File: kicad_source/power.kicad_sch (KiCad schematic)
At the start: 45 parts, among them CN1 DNI, CN2 SM04B-GHS-TB, CN3 SM04B-GHS-TB, CN4 Powerpole_2, CN5 SM04B-GHS-TB, CN6 SM04B-GHS-TB, CN7 DNI, U1 RAA211650

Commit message: reworked schematic
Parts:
- removed C11, C9: 100 nF, Capacitor_SMD:C_0603_1608Metric, symbol Device:C_Small
- removed CN2, CN3, CN5, CN6: SM04B-GHS-TB, Connector_JST:JST_GH_SM04B-GHS-TB_1x04-1MP_P1.25mm_Horizontal, symbol Connector_Generic_MountingPin:Conn_01x04_MountingPin
- removed D1, D2: B520C, Diode_SMD:D_SMC, symbol Device:D_Schottky_Small
- removed H1, H2, H3, H4: MountingHole_Pad, MountingHole:MountingHole_3.2mm_M3_DIN965_Pad, symbol Mechanical:MountingHole_Pad
- removed L2: Label, generationmake:generationmake_logo, symbol generationmake:Label
- removed L3: Label, generationmake:generationmake_small_solder, symbol generationmake:Label
- removed L4: Label, generationmake:opencyphal_small, symbol generationmake:Label
- added D?: MBR0530T1G, Diode_SMD:D_SOD-123, symbol Device:D_Schottky_Small
- renumbered C17 to C13, C1 to C14, C2 to C15, C3 to C16, C12 to C17, C4 to C18, C13 to C19, C5 to C20, C6 to C21, C14 to C22, C15 to C23, C7 to C24, C16 to C25, C8 to C26, C10 to C27, CN1 to CN10, CN7 to CN13, CN4 to CN9, D4 to D1, L1 to L4, R5 to R26, R6 to R27, R1 to R28, R2 to R29, R3 to R30, R7 to R31, R8 to R32, R4 to R33
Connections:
- net VCC: now also D?.2 (A)
- new net +5V: D?.1 (K)
- no-connect marks 4 -> 0
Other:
- note added: "30V 500mA"
- company: 107-systems -> generationmake
- title: l3xz-hw_can_power_injector -> OpenCyphalServoController12
- moved on the sheet: C26, C27, D3, R33

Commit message: started first placement
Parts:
- removed C23: 220 uF / 50 V, Capacitor_SMD:CP_Elec_10x10, symbol Device:C_Polarized_Small
- C13: renamed from C17; value 220 uF / 50 V -> 100 uF / 50 V; footprint Capacitor_SMD:CP_Elec_10x10 -> Capacitor_SMD:CP_Elec_8x10
- C15: renamed from C19; value 220 uF / 50 V -> 100 uF / 50 V; footprint Capacitor_SMD:CP_Elec_10x10 -> Capacitor_SMD:CP_Elec_8x10
- gave numbers to parts that had none: 1
- renumbered C14 to C10, C15 to C11, C16 to C12, C18 to C14, C20 to C16, C21 to C17, C22 to C18, C24 to C20, C25 to C21, C26 to C22, C27 to C23, C13 to C9, CN9 to CN12, CN10 to CN13, CN13 to CN14, D1 to D4, D3 to D5, U1 to U4
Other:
- note added: "ECC ZA500101MHA"
- note removed: "ECC MZL500ARA221 EMZL500ARA221MJA0G"

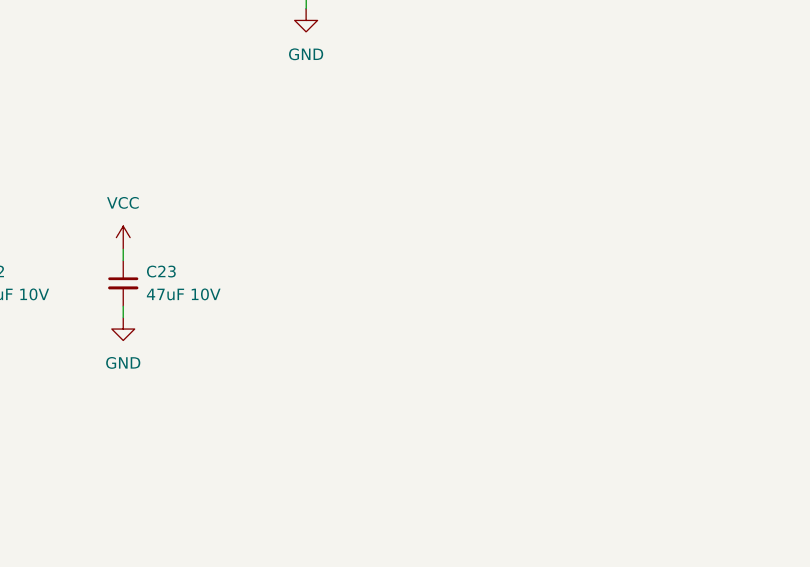
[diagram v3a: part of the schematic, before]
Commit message: added additional capacitors on VCC
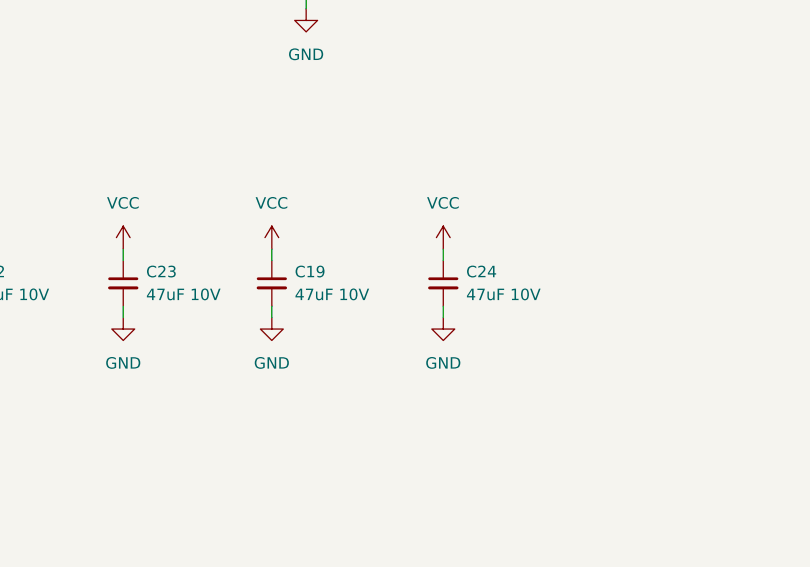
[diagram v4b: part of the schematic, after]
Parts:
- added C19, C24: 47uF 10V, Capacitor_SMD:C_1210_3225Metric, symbol Device:C_Small
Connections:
- net GND: now also C19.2, C24.2
- net VCC: now also C19.1, C24.1
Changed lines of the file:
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@@
+    (stroke (width 0) (type default) (color 0 0 0 0))
+  )
+  (wire (pts (xy 207.01 71.12) (xy 207.01 72.39))
     (stroke (width 0) (type default) (color 0 0 0 0))
   )
@@
     (stroke (width 0) (type default) (color 0 0 0 0))
   )
+  (wire (pts (xy 187.96 71.12) (xy 187.96 72.39))
+    (stroke (width 0) (type default) (color 0 0 0 0))
+  )
   (wire (pts (xy 86.36 24.13) (xy 86.36 25.4))
     (stroke (width 0) (type default) (color 0 0 0 0))
@@
     (stroke (width 0) (type default) (color 0 0 0 0))
   )
+  (wire (pts (xy 207.01 77.47) (xy 207.01 78.74))
+    (stroke (width 0) (type default) (color 0 0 0 0))
+  )
   (wire (pts (xy 86.36 30.48) (xy 86.36 31.75))
     (stroke (width 0) (type default) (color 0 0 0 0))
@@
   )
   (wire (pts (xy 100.33 87.63) (xy 97.79 87.63))
+    (stroke (width 0) (type default) (color 0 0 0 0))
+  )
+  (wire (pts (xy 187.96 77.47) (xy 187.96 78.74))
     (stroke (width 0) (type default) (color 0 0 0 0))
   )
@@
     (pin "1")
   )
+  (symbol (lib_id "power:VCC") (at 187.96 71.12 0) (unit 1)
+    (in_bom yes) (on_board yes) (fields_autoplaced)
+    (property "Reference" "#PWR088" (id 0) (at 187.96 74.93 0)
+      (effects (font (size 1.27 1.27)) hide)
+    )
+    (property "Value" "VCC" (id 1) (at 187.96 66.04 0))
+    (property "Footprint" "" (id 2) (at 187.96 71.12 0)
+      (effects (font (size 1.27 1.27)) hide)
+    )
+    (property "Datasheet" "" (id 3) (at 187.96 71.12 0)
+      (effects (font (size 1.27 1.27)) hide)
+    )
+    (pin "1")
+  )
   (symbol (lib_id "power:GND") (at 97.79 100.33 0) (unit 1)
     (in_bom yes) (on_board yes) (fields_autoplaced)
@@
     (pin "1")
   )
+  (symbol (lib_id "power:GND") (at 207.01 78.74 0) (unit 1)
+    (in_bom yes) (on_board yes) (fields_autoplaced)
+    (property "Reference" "#PWR0105" (id 0) (at 207.01 85.09 0)
+      (effects (font (size 1.27 1.27)) hide)
+    )
+    (property "Value" "GND" (id 1) (at 207.01 83.82 0))
+    (property "Footprint" "" (id 2) (at 207.01 78.74 0)
+      (effects (font (size 1.27 1.27)) hide)
+    )
+    (property "Datasheet" "" (id 3) (at 207.01 78.74 0)
+      (effects (font (size 1.27 1.27)) hide)
+    )
+    (pin "1")
+  )
   (symbol (lib_id "Device:C_Small") (at 118.11 44.45 0) (unit 1)
     (in_bom yes) (on_board yes) (fields_autoplaced)
@@
     )
     (property "Datasheet" "" (id 3) (at 54.61 57.15 0)
+      (effects (font (size 1.27 1.27)) hide)
+    )
+    (pin "1")
+  )
+  (symbol (lib_id "power:GND") (at 187.96 78.74 0) (unit 1)
+    (in_bom yes) (on_board yes) (fields_autoplaced)
+    (property "Reference" "#PWR089" (id 0) (at 187.96 85.09 0)
+      (effects (font (size 1.27 1.27)) hide)
+    )
+    (property "Value" "GND" (id 1) (at 187.96 83.82 0))
+    (property "Footprint" "" (id 2) (at 187.96 78.74 0)
+      (effects (font (size 1.27 1.27)) hide)
+    )
+    (property "Datasheet" "" (id 3) (at 187.96 78.74 0)
       (effects (font (size 1.27 1.27)) hide)
     )
@@
     (pin "1")
     (pin "2")
+  )
+  (symbol (lib_id "power:VCC") (at 207.01 71.12 0) (unit 1)
+    (in_bom yes) (on_board yes) (fields_autoplaced)
+    (property "Reference" "#PWR0104" (id 0) (at 207.01 74.93 0)
+      (effects (font (size 1.27 1.27)) hide)
+    )
+    (property "Value" "VCC" (id 1) (at 207.01 66.04 0))
+    (property "Footprint" "" (id 2) (at 207.01 71.12 0)
+      (effects (font (size 1.27 1.27)) hide)
+    )
+    (property "Datasheet" "" (id 3) (at 207.01 71.12 0)
+      (effects (font (size 1.27 1.27)) hide)
+    )
+    (pin "1")
   )
   (symbol (lib_id "power:GND") (at 107.95 31.75 0) (unit 1)
@@
     (pin "2")
   )
+  (symbol (lib_id "Device:C_Small") (at 187.96 74.93 0) (unit 1)
+    (in_bom yes) (on_board yes) (fields_autoplaced)
+    (property "Reference" "C19" (id 0) (at 190.5 73.6662 0)
+      (effects (font (size 1.27 1.27)) (justify left))
+    )
+    (property "Value" "47uF 10V" (id 1) (at 190.5 76.2062 0)
+      (effects (font (size 1.27 1.27)) (justify left))
+    )
+    (property "Footprint" "Capacitor_SMD:C_1210_3225Metric" (id 2) (at 187.96 74.93 0)
+      (effects (font (size 1.27 1.27)) hide)
+    )
+    (property "Datasheet" "~" (id 3) (at 187.96 74.93 0)
+      (effects (font (size 1.27 1.27)) hide)
+    )
+    (pin "1")
+    (pin "2")
+  )
   (symbol (lib_id "power:GND") (at 55.88 93.98 0) (unit 1)
     (in_bom yes) (on_board yes) (fields_autoplaced)
@@
       (effects (font (size 1.27 1.27)) hide)
     )
+    (pin "1")
+    (pin "2")
+  )
+  (symbol (lib_id "Device:C_Small") (at 207.01 74.93 0) (unit 1)
+    (in_bom yes) (on_board yes) (fields_autoplaced)
+    (property "Reference" "C24" (id 0) (at 209.55 73.6662 0)
+      (effects (font (size 1.27 1.27)) (justify left))
+    )
+    (property "Value" "47uF 10V" (id 1) (at 209.55 76.2062 0)
+      (effects (font (size 1.27 1.27)) (justify left))
+    )
+    (property "Footprint" "Capacitor_SMD:C_1210_3225Metric" (id 2) (at 207.01 74.93 0)
+      (effects (font (size 1.27 1.27)) hide)
+    )
+    (property "Datasheet" "~" (id 3) (at 207.01 74.93 0)
+      (effects (font (size 1.27 1.27)) hide)
+    )

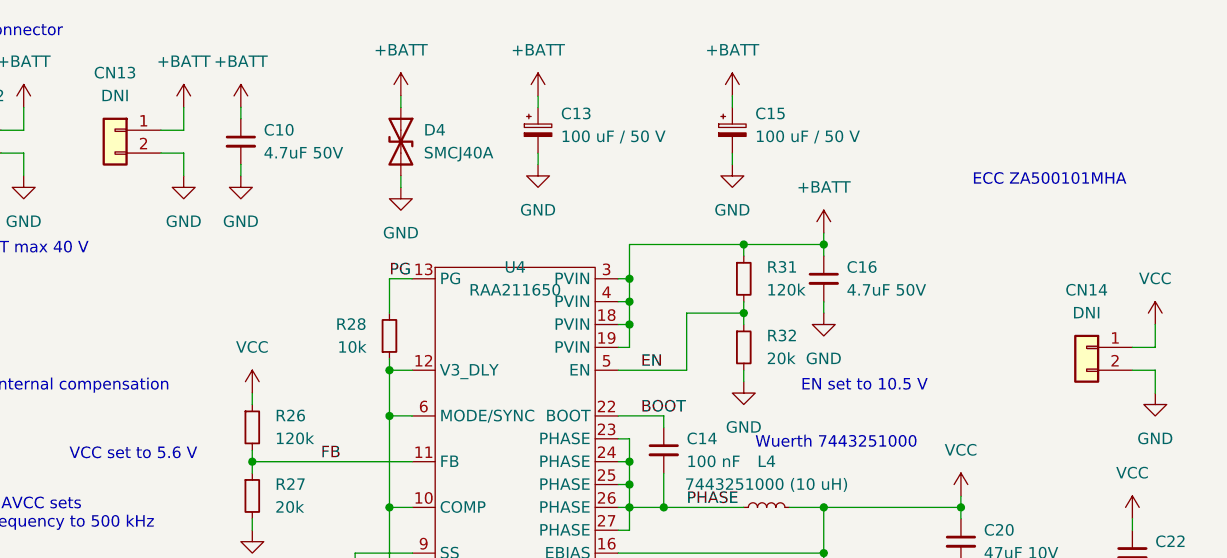
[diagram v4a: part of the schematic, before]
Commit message: added enable and power good for voltage regulator
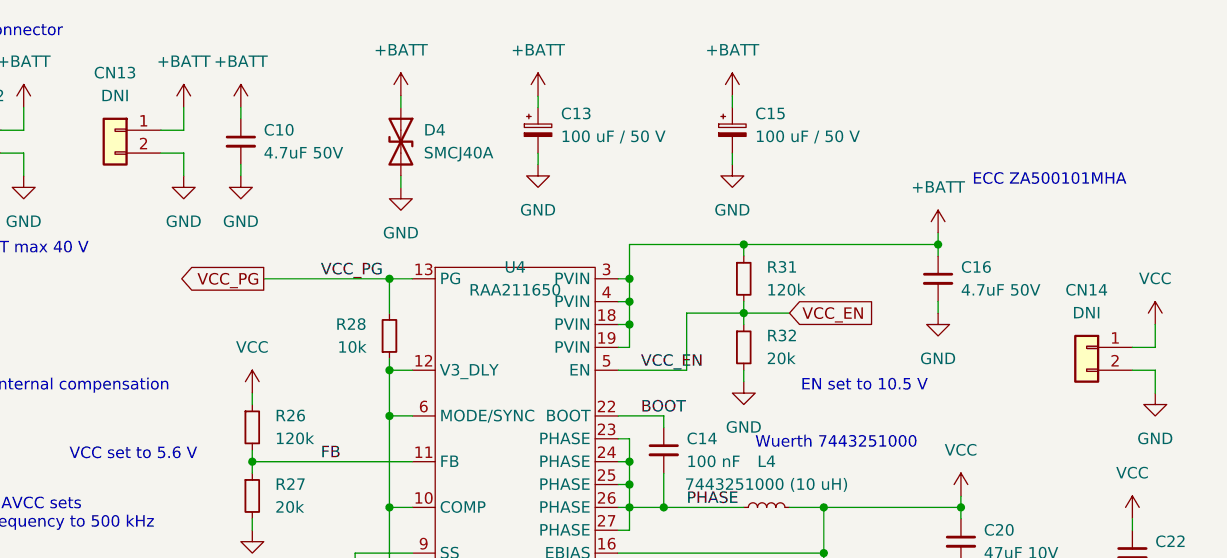
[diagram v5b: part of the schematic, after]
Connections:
- net EN renamed VCC_EN
- net PG renamed VCC_PG
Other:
- moved on the sheet: C16
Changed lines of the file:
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@@
   (junction (at 69.85 80.01) (diameter 0) (color 0 0 0 0)
   )
-  (junction (at 118.11 40.64) (diameter 0) (color 0 0 0 0)
+  (junction (at 130.81 40.64) (diameter 0) (color 0 0 0 0)
   )
   (junction (at 97.79 90.17) (diameter 0) (color 0 0 0 0)
@@
   (junction (at 118.11 69.85) (diameter 0) (color 0 0 0 0)
   )
+  (junction (at 100.33 69.85) (diameter 0) (color 0 0 0 0)
+  )
+  (junction (at 96.52 44.45) (diameter 0) (color 0 0 0 0)
+  )
+  (junction (at 96.52 64.77) (diameter 0) (color 0 0 0 0)
+  )
+  (junction (at 97.79 87.63) (diameter 0) (color 0 0 0 0)
+  )
+  (junction (at 69.85 44.45) (diameter 0) (color 0 0 0 0)
+  )
+  (junction (at 96.52 67.31) (diameter 0) (color 0 0 0 0)
+  )
+  (junction (at 133.35 69.85) (diameter 0) (color 0 0 0 0)
+  )
+  (junction (at 97.79 95.25) (diameter 0) (color 0 0 0 0)
+  )
+  (junction (at 69.85 59.69) (diameter 0) (color 0 0 0 0)
+  )
+  (junction (at 118.11 74.93) (diameter 0) (color 0 0 0 0)
+  )
+  (junction (at 97.79 85.09) (diameter 0) (color 0 0 0 0)
+  )
+  (junction (at 97.79 92.71) (diameter 0) (color 0 0 0 0)
+  )
+  (junction (at 97.79 97.79) (diameter 0) (color 0 0 0 0)
+  )
   (junction (at 109.22 40.64) (diameter 0) (color 0 0 0 0)
   )
-  (junction (at 100.33 69.85) (diameter 0) (color 0 0 0 0)
-  )
-  (junction (at 96.52 44.45) (diameter 0) (color 0 0 0 0)
-  )
-  (junction (at 96.52 64.77) (diameter 0) (color 0 0 0 0)
-  )
-  (junction (at 97.79 87.63) (diameter 0) (color 0 0 0 0)
-  )
-  (junction (at 96.52 67.31) (diameter 0) (color 0 0 0 0)
-  )
-  (junction (at 133.35 69.85) (diameter 0) (color 0 0 0 0)
-  )
-  (junction (at 97.79 95.25) (diameter 0) (color 0 0 0 0)
-  )
-  (junction (at 69.85 59.69) (diameter 0) (color 0 0 0 0)
-  )
-  (junction (at 118.11 74.93) (diameter 0) (color 0 0 0 0)
-  )
-  (junction (at 97.79 85.09) (diameter 0) (color 0 0 0 0)
-  )
-  (junction (at 97.79 92.71) (diameter 0) (color 0 0 0 0)
-  )
-  (junction (at 97.79 97.79) (diameter 0) (color 0 0 0 0)
-  )
   (junction (at 96.52 46.99) (diameter 0) (color 0 0 0 0)
   )
@@
     (stroke (width 0) (type default) (color 0 0 0 0))
   )
-  (wire (pts (xy 118.11 40.64) (xy 118.11 41.91))
+  (wire (pts (xy 130.81 40.64) (xy 130.81 41.91))
     (stroke (width 0) (type default) (color 0 0 0 0))
   )
@@
     (stroke (width 0) (type default) (color 0 0 0 0))
   )
-  (wire (pts (xy 118.11 46.99) (xy 118.11 48.26))
+  (wire (pts (xy 130.81 46.99) (xy 130.81 48.26))
     (stroke (width 0) (type default) (color 0 0 0 0))
   )
@@
     (stroke (width 0) (type default) (color 0 0 0 0))
   )
+  (wire (pts (xy 109.22 48.26) (xy 114.3 48.26))
+    (stroke (width 0) (type default) (color 0 0 0 0))
+  )
   (wire (pts (xy 55.88 85.09) (xy 69.85 85.09))
     (stroke (width 0) (type default) (color 0 0 0 0))
@@
     (stroke (width 0) (type default) (color 0 0 0 0))
   )
+  (wire (pts (xy 55.88 44.45) (xy 69.85 44.45))
+    (stroke (width 0) (type default) (color 0 0 0 0))
+  )
   (wire (pts (xy 118.11 74.93) (xy 118.11 76.2))
     (stroke (width 0) (type default) (color 0 0 0 0))
@@
     (stroke (width 0) (type default) (color 0 0 0 0))
   )
-  (wire (pts (xy 118.11 39.37) (xy 118.11 40.64))
+  (wire (pts (xy 130.81 39.37) (xy 130.81 40.64))
     (stroke (width 0) (type default) (color 0 0 0 0))
   )
@@
     (stroke (width 0) (type default) (color 0 0 0 0))
   )
-  (wire (pts (xy 109.22 40.64) (xy 118.11 40.64))
+  (wire (pts (xy 109.22 40.64) (xy 130.81 40.64))
     (stroke (width 0) (type default) (color 0 0 0 0))
   )
@@
     (effects (font (size 1.27 1.27)) (justify left bottom))
   )
-  (label "EN" (at 97.79 54.61 0)
+  (label "VCC_EN" (at 97.79 54.61 0)
     (effects (font (size 1.27 1.27)) (justify left bottom))
   )
@@
     (effects (font (size 1.27 1.27)) (justify left bottom))
   )
-  (label "PG" (at 69.85 44.45 0)
+  (label "VCC_PG" (at 62.23 44.45 0)
     (effects (font (size 1.27 1.27)) (justify left bottom))
   )
@@
   (label "SS" (at 57.15 81.28 0)
     (effects (font (size 1.27 1.27)) (justify left bottom))
+  )
+  (global_label "VCC_PG" (shape output) (at 55.88 44.45 180) (fields_autoplaced)
+    (effects (font (size 1.27 1.27)) (justify right))
+    (property "Referenzen zwischen Schaltplänen" "${INTERSHEET_REFS}" (id 0) (at 46.4196 44.3706 0)
+      (effects (font (size 1.27 1.27)) (justify right) hide)
+    )
+  )
+  (global_label "VCC_EN" (shape input) (at 114.3 48.26 0) (fields_autoplaced)
+    (effects (font (size 1.27 1.27)) (justify left))
+    (property "Referenzen zwischen Schaltplänen" "${INTERSHEET_REFS}" (id 0) (at 123.6999 48.1806 0)
+      (effects (font (size 1.27 1.27)) (justify left) hide)
+    )
   )
   (symbol (lib_id "Device:C_Small") (at 55.88 90.17 0) (mirror x) (unit 1)
@@
     (pin "2")
   )
-  (symbol (lib_id "power:GND") (at 118.11 48.26 0) (unit 1)
-    (in_bom yes) (on_board yes) (fields_autoplaced)
-    (property "Reference" "#PWR084" (id 0) (at 118.11 54.61 0)
-      (effects (font (size 1.27 1.27)) hide)
-    )
-    (property "Value" "GND" (id 1) (at 118.11 53.34 0))
-    (property "Footprint" "" (id 2) (at 118.11 48.26 0)
-      (effects (font (size 1.27 1.27)) hide)
-    )
-    (property "Datasheet" "" (id 3) (at 118.11 48.26 0)
+  (symbol (lib_id "power:GND") (at 130.81 48.26 0) (unit 1)
+    (in_bom yes) (on_board yes) (fields_autoplaced)
+    (property "Reference" "#PWR084" (id 0) (at 130.81 54.61 0)
+      (effects (font (size 1.27 1.27)) hide)
+    )
+    (property "Value" "GND" (id 1) (at 130.81 53.34 0))
+    (property "Footprint" "" (id 2) (at 130.81 48.26 0)
+      (effects (font (size 1.27 1.27)) hide)
+    )
+    (property "Datasheet" "" (id 3) (at 130.81 48.26 0)
       (effects (font (size 1.27 1.27)) hide)
     )
@@
     (pin "1")
   )
-  (symbol (lib_id "Device:C_Small") (at 118.11 44.45 0) (unit 1)
-    (in_bom yes) (on_board yes) (fields_autoplaced)
-    (property "Reference" "C16" (id 0) (at 120.65 43.1862 0)
-      (effects (font (size 1.27 1.27)) (justify left))
-    )
-    (property "Value" "4.7uF 50V" (id 1) (at 120.65 45.7262 0)
-      (effects (font (size 1.27 1.27)) (justify left))
-    )
-    (property "Footprint" "Capacitor_SMD:C_1210_3225Metric" (id 2) (at 118.11 44.45 0)
-      (effects (font (size 1.27 1.27)) hide)
-    )
-    (property "Datasheet" "~" (id 3) (at 118.11 44.45 0)
+  (symbol (lib_id "Device:C_Small") (at 130.81 44.45 0) (unit 1)
+    (in_bom yes) (on_board yes) (fields_autoplaced)
+    (property "Reference" "C16" (id 0) (at 133.35 43.1862 0)
+      (effects (font (size 1.27 1.27)) (justify left))
+    )
+    (property "Value" "4.7uF 50V" (id 1) (at 133.35 45.7262 0)
+      (effects (font (size 1.27 1.27)) (justify left))
+    )
+    (property "Footprint" "Capacitor_SMD:C_1210_3225Metric" (id 2) (at 130.81 44.45 0)
+      (effects (font (size 1.27 1.27)) hide)
+    )
+    (property "Datasheet" "~" (id 3) (at 130.81 44.45 0)
       (effects (font (size 1.27 1.27)) hide)
     )
@@
     (pin "1")
   )
-  (symbol (lib_id "power:+BATT") (at 118.11 39.37 0) (unit 1)
-    (in_bom yes) (on_board yes) (fields_autoplaced)
-    (property "Reference" "#PWR083" (id 0) (at 118.11 43.18 0)
-      (effects (font (size 1.27 1.27)) hide)
-    )
-    (property "Value" "+BATT" (id 1) (at 118.11 34.29 0))
-    (property "Footprint" "" (id 2) (at 118.11 39.37 0)
-      (effects (font (size 1.27 1.27)) hide)
-    )
-    (property "Datasheet" "" (id 3) (at 118.11 39.37 0)
-      (effects (font (size 1.27 1.27)) hide)
-    )
+  (symbol (lib_id "power:+BATT") (at 130.81 39.37 0) (unit 1)
+    (in_bom yes) (on_board yes) (fields_autoplaced)
+    (property "Reference" "#PWR083" (id 0) (at 130.81 43.18 0)
+      (effects (font (size 1.27 1.27)) hide)
+    )
+    (property "Value" "+BATT" (id 1) (at 130.81 34.29 0))
+    (property "Footprint" "" (id 2) (at 130.81 39.37 0)
+      (effects (font (size 1.27 1.27)) hide)
+    )
+    (property "Datasheet" "" (id 3) (at 130.81 39.37 0)
+      (effects (font (size 1.27 1.27)) hide)
+    )
